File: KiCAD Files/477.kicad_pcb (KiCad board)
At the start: 2 copper layers, 53 parts, among them IC1 W25N01GVSFIG, IC2 W25N01GVSFIG, IC3 W25N01GVSFIG, IC4 W25N01GVSFIG, IC5 AZ1117IH-3.3TRG1, J1 BM06B-SRSS-TBT_LF__SN_, J2 6364372-2, J3 TSW-103-14-S-D, J4 TSW-103-14-S-D, U1 STM32H7A3RGTx, Y1 ABM8G-48.000MHZ-18-D2Y-T

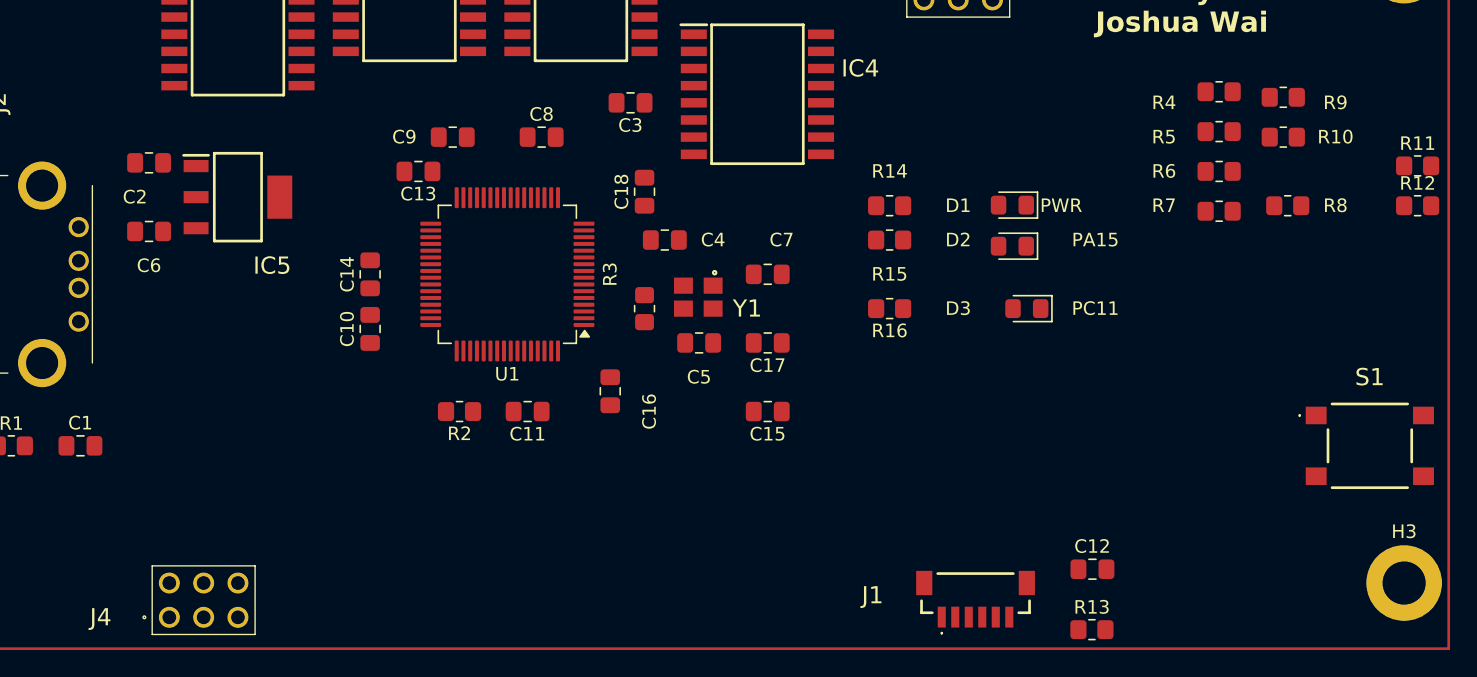
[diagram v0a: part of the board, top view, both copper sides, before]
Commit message: added additional connector
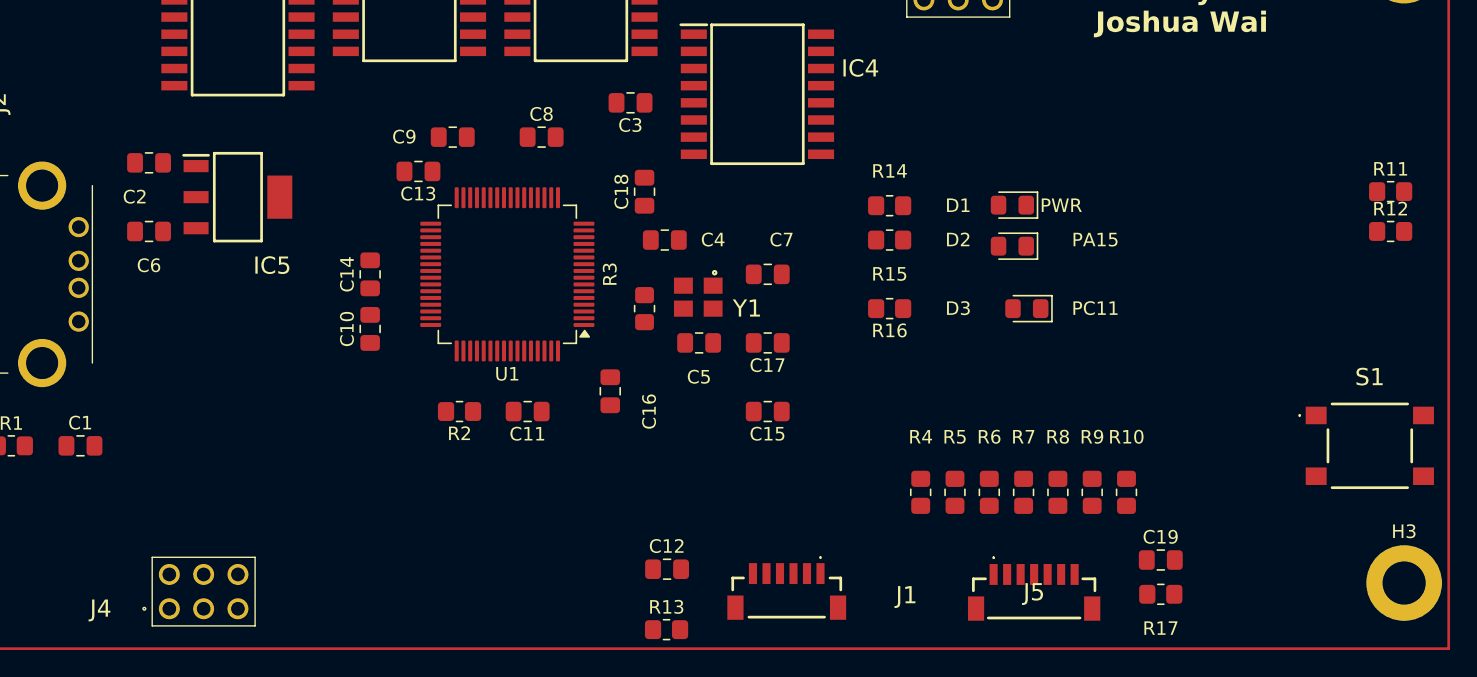
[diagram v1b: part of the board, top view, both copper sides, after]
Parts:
- added C19: 2.2n, Capacitor_SMD:C_0805_2012Metric_Pad1.18x1.45mm_HandSolder, F.Cu at (144.5, 110.7)
- added J5: BM07B-SRSS-TB_LF__SN_, CustomFootprints:BM07BSRSSTBLFSN, F.Cu at (135.2, 113.5)
- added R17: 1M, Resistor_SMD:R_0805_2012Metric_Pad1.20x1.40mm_HandSolder, F.Cu at (144.5, 113.2)
- C3: value C -> 0.1u
- moved R4 37.0 mm to (126.8, 105.7), turned to 90 degrees
- moved R5 33.1 mm to (129.3, 105.7), turned to 90 degrees
- moved R9 32.5 mm to (139.5, 105.7), turned to 90 degrees
- moved R13 31.5 mm to (107.9, 115.8)
- moved C12 31.5 mm to (108.0, 111.4)
- moved R6 29.2 mm to (131.8, 105.7), turned to 90 degrees
- moved R10 28.8 mm to (142.0, 105.7), turned to -90 degrees
- moved R8 27.2 mm to (136.9, 105.7), turned to -90 degrees
- moved R7 25.4 mm to (134.4, 105.7), turned to -90 degrees
- moved J1 14.0 mm to (116.8, 113.3), turned to 180 degrees
- moved R11 2.76 mm to (161.6, 83.4)
- moved R12 2.76 mm to (161.6, 86.4)
- moved J4 0.64 mm to (71.1, 114.3)
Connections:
- J1 pad 2: GND -> PC0/Touch Out
- J1 pad 3: PD2/FP RX -> VBAT
- J1 pad 5: VBAT -> PD2/FP RX
- J4 pad 1: unconnected-(J4-Pad1) -> PC0/Touch Out
- R10 pad 1: Net-(U7-Col3) -> PB6/KeyC3
- R10 pad 2: PB6/KeyC3 -> Net-(J5-Pad7)
- R7 pad 1: Net-(U7-Row4) -> PB3/KeyR4
- R7 pad 2: PB3/KeyR4 -> Net-(J5-Pad4)
- R8 pad 1: Net-(U7-Col1) -> PB4/KeyC1
- R8 pad 2: PB4/KeyC1 -> Net-(J5-Pad5)
- U1 pad 8: unconnected-(U1-PC0-Pad8) -> PC0/Touch Out

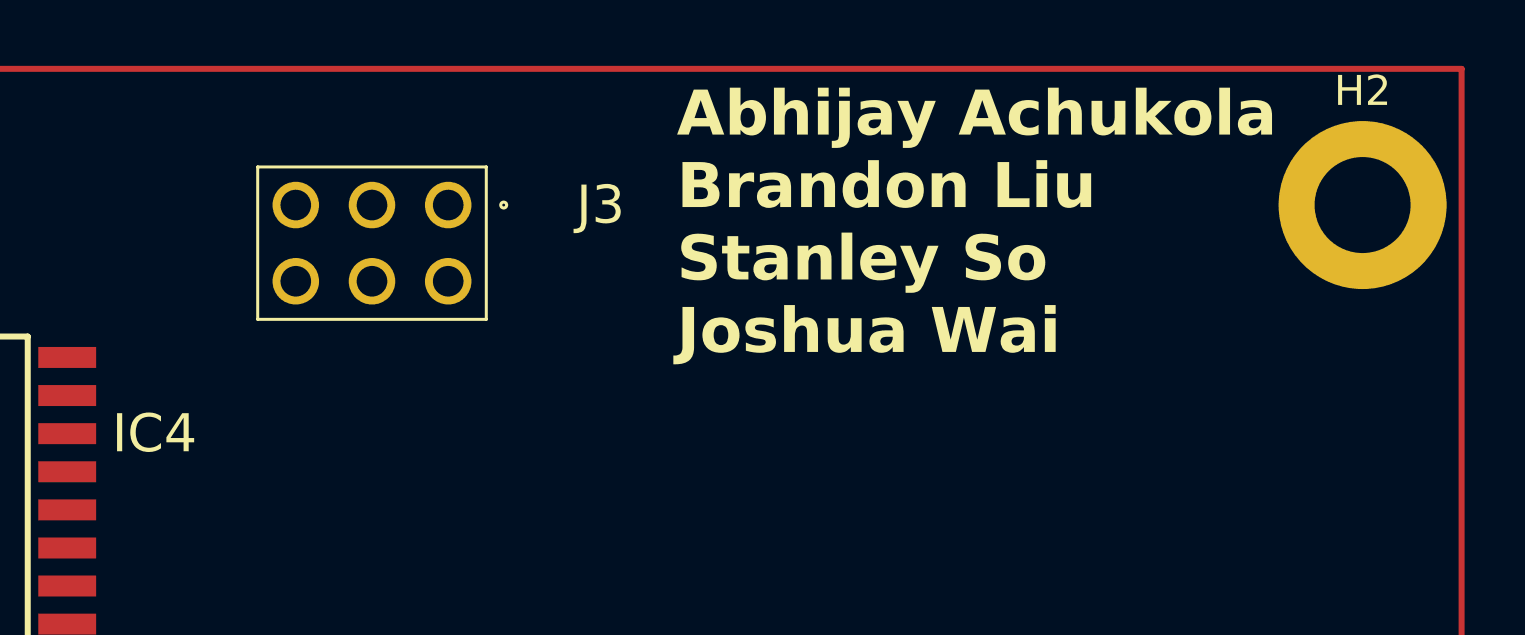
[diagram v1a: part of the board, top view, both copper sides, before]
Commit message: modified silkscreen
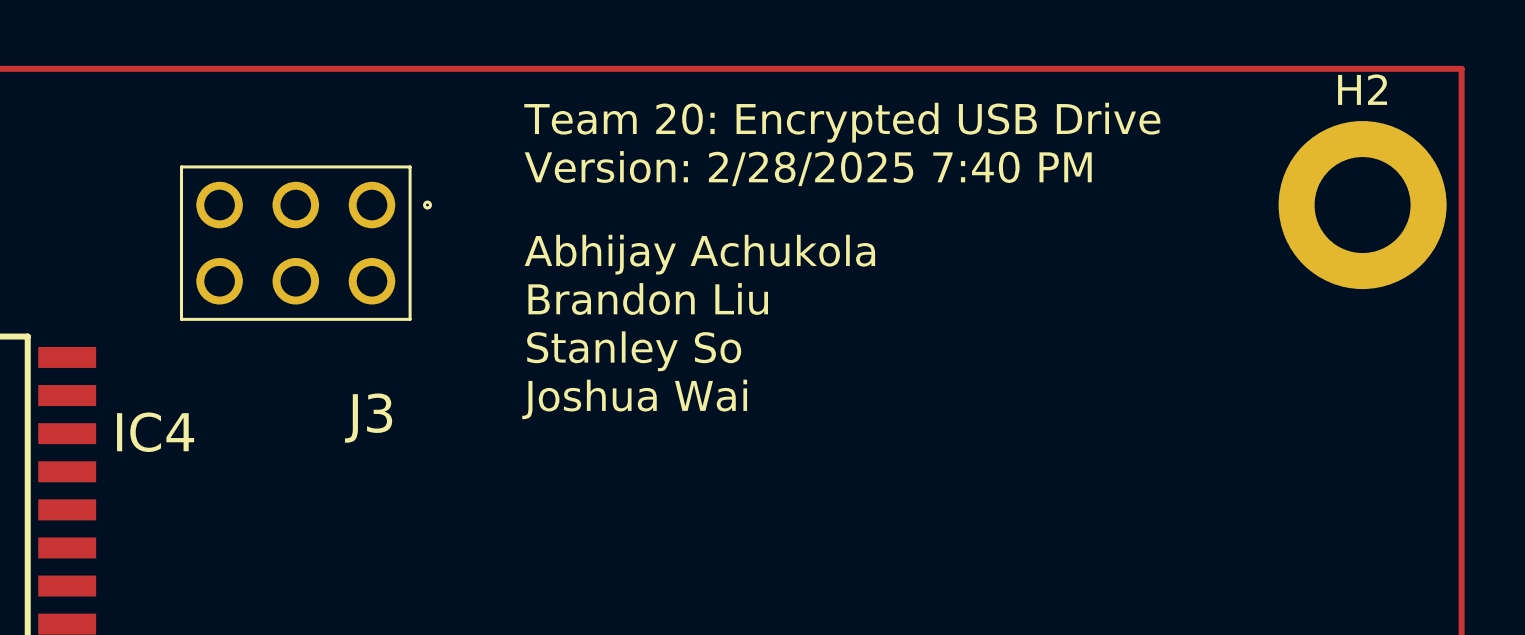
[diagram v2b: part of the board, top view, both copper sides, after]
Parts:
- moved J3 2.54 mm to (129.5, 66.7)
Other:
- board text added: "Team 20: Encrypted USB Drive Version: 2/28/2025 7:40 PM"
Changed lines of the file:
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@@
 	(footprint "CustomFootprints:custom1"
 		(layer "F.Cu")
-		(at 132.08 66.675 180)
+		(at 129.54 66.675 180)
 		(descr "TSW-103-XX-YY-D")
 		(tags "Connector")
 		(property "Reference" "J3"
-			(at -5.08 0 360)
+			(at 0 -6.985 360)
 			(layer "F.SilkS")
 			(effects
@@
 		)
 	)
-	(gr_text "Abhijay Achukola\nBrandon Liu\nStanley So \nJoshua Wai"
-		(at 139.7 71.755 0)
+	(gr_text "Team 20: Encrypted USB Drive\nVersion: 2/28/2025 7:40 PM\n"
+		(at 134.62 66.04 0)
 		(layer "F.SilkS")
 		(effects
 			(font
-				(size 1.5 1.5)
-				(thickness 0.3)
-				(bold yes)
+				(size 1 1)
+				(thickness 0.1875)
 			)
 			(justify left bottom)
@@
 		)
 	)
+	(gr_text "\nAbhijay Achukola\nBrandon Liu\nStanley So \nJoshua Wai"
+		(at 134.62 73.66 0)
+		(layer "F.SilkS")
+		(effects
+			(font
+				(size 1 1)
+				(thickness 0.125)
+			)
+			(justify left bottom)
+		)
+	)

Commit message: found final connector
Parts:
- removed R12: R_US, Resistor_SMD:R_0805_2012Metric_Pad1.20x1.40mm_HandSolder
- added C20: 2.2n, Capacitor_SMD:C_0805_2012Metric_Pad1.18x1.45mm_HandSolder, F.Cu at (138.9, 89.0)
- added J6: BM09B-SRSS-TB_LF__SN_, CustomFootprints:BM09BSRSSTBLFSN, F.Cu at (142.2, 78.7)
- R11: value R_US -> 1M
- moved S1 83.9 mm to (76.2, 99.1)
- moved H2 20.3 mm to (142.2, 66.0)
- moved H3 20.3 mm to (142.2, 111.8)
- moved R11 19.4 mm to (143.0, 89.0)
- moved C12 19.1 mm to (88.9, 109.8)
- moved J1 19.1 mm to (97.8, 111.8)
- moved R13 19.1 mm to (88.9, 114.3)
- moved J5 13.4 mm to (121.9, 111.8)
- moved C19 13.4 mm to (131.3, 108.9)
- moved R17 13.4 mm to (131.3, 111.5)
- moved R14 12.2 mm to (132.1, 94.0), turned to 90 degrees
- moved R5 10.1 mm to (119.4, 103.9)
- moved R9 10.1 mm to (129.5, 103.9)
- moved R4 10.1 mm to (116.8, 103.9)
- moved R6 10.1 mm to (121.9, 103.9)
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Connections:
- R11 pad 1: VBAT -> Net-(C20-Pad1)
- R11 pad 2: Net-(DS1-VO) -> GND
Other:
- board text added: "Team 20: Encrypted USB Drive Version: 2/28/2025 9:35 PM"
- board text removed: "Team 20: Encrypted USB Drive Version: 2/28/2025 7:40 PM"

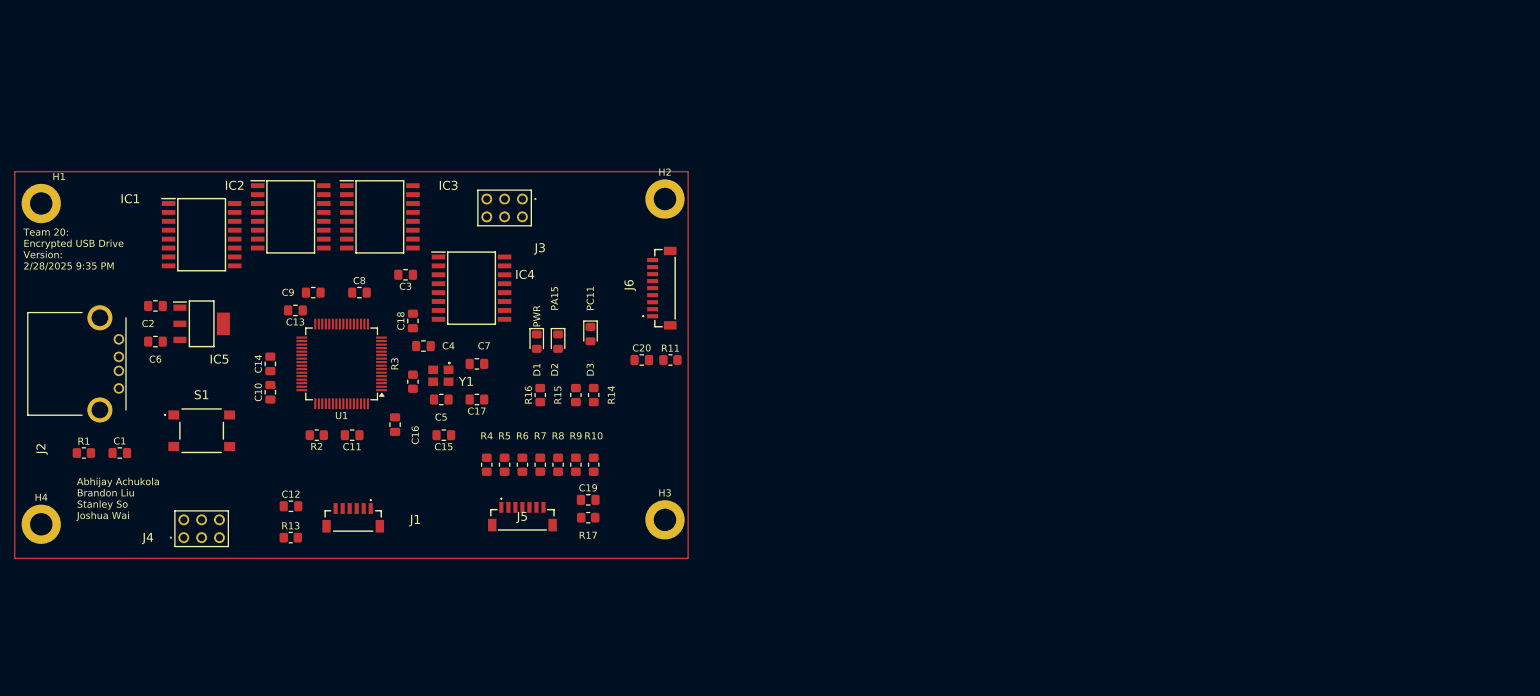
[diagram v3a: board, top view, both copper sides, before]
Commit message: finalized schematic
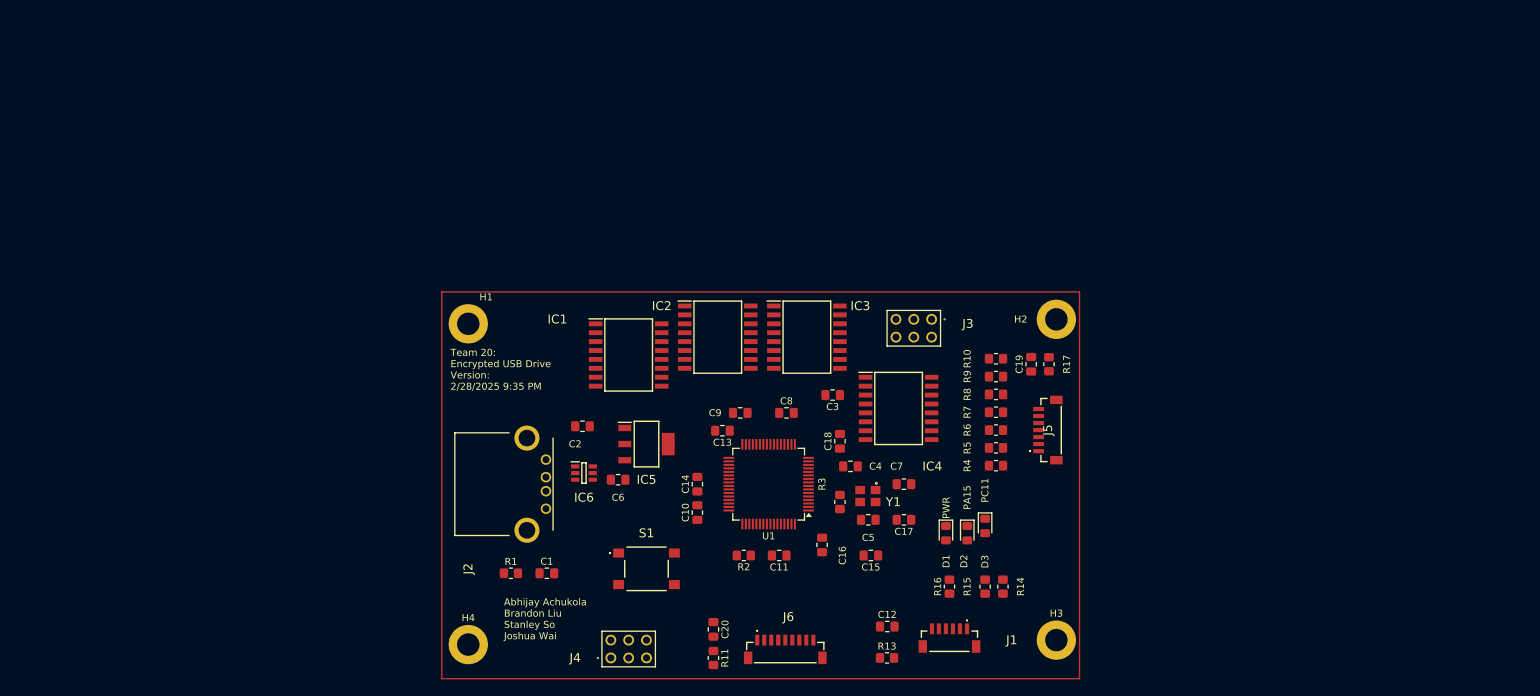
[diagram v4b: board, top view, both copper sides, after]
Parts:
- added IC6: USBLC6-2SC6, CustomFootprints:SOT95P280X145-6N, F.Cu at (130.7, 105.1)
- R14, R15, R16: value R_US -> 220
- R2: value R_US -> 10k
- moved C12 86.7 mm to (173.9, 127.0)
- moved J1 86.7 mm to (182.8, 128.9)
- moved R13 86.7 mm to (173.9, 131.4)
- moved J5 76.4 mm to (197.3, 99.0), turned to 90 degrees
- moved R4 72.6 mm to (189.4, 104.0), turned to 180 degrees
- moved R5 70.1 mm to (189.4, 101.5), turned to 180 degrees
- moved R17 69.2 mm to (197.0, 89.6), turned to 90 degrees
- moved C6 68.8 mm to (135.6, 106.0)
- moved R6 67.7 mm to (189.4, 99.0), turned to 180 degrees
- moved S1 66.4 mm to (139.6, 118.7)
- moved C19 66.0 mm to (194.4, 89.6), turned to 90 degrees
- moved IC5 65.7 mm to (139.6, 101.0)
- moved R7 65.4 mm to (189.4, 96.4), turned to 0 degrees
- moved D1 64.4 mm to (182.3, 113.7)
- moved R15 64.4 mm to (187.9, 121.3)
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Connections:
- J2 pad 2: PA11/USB- -> Net-(IC6-I/O1_1)
- J2 pad 3: PA12/USB+ -> Net-(IC6-I/O2_1)

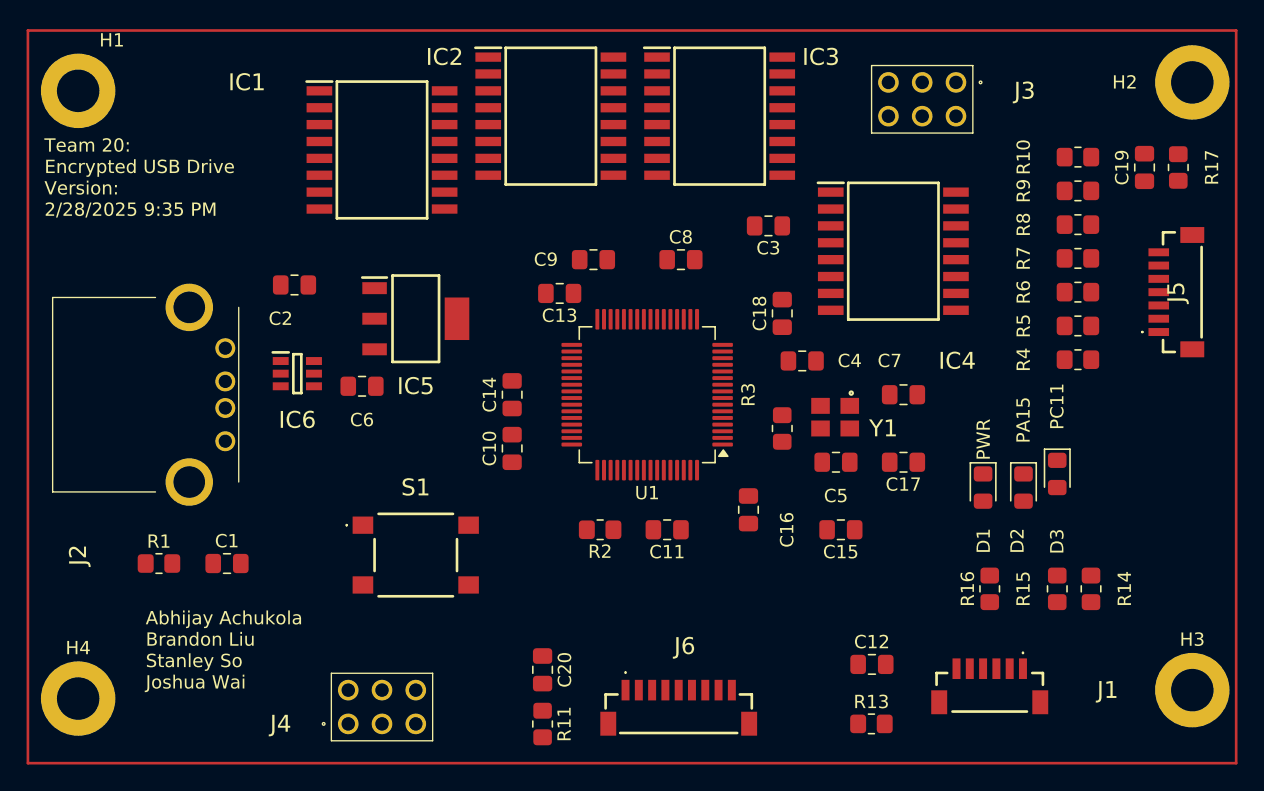
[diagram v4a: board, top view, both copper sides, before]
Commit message: modified mounting holes
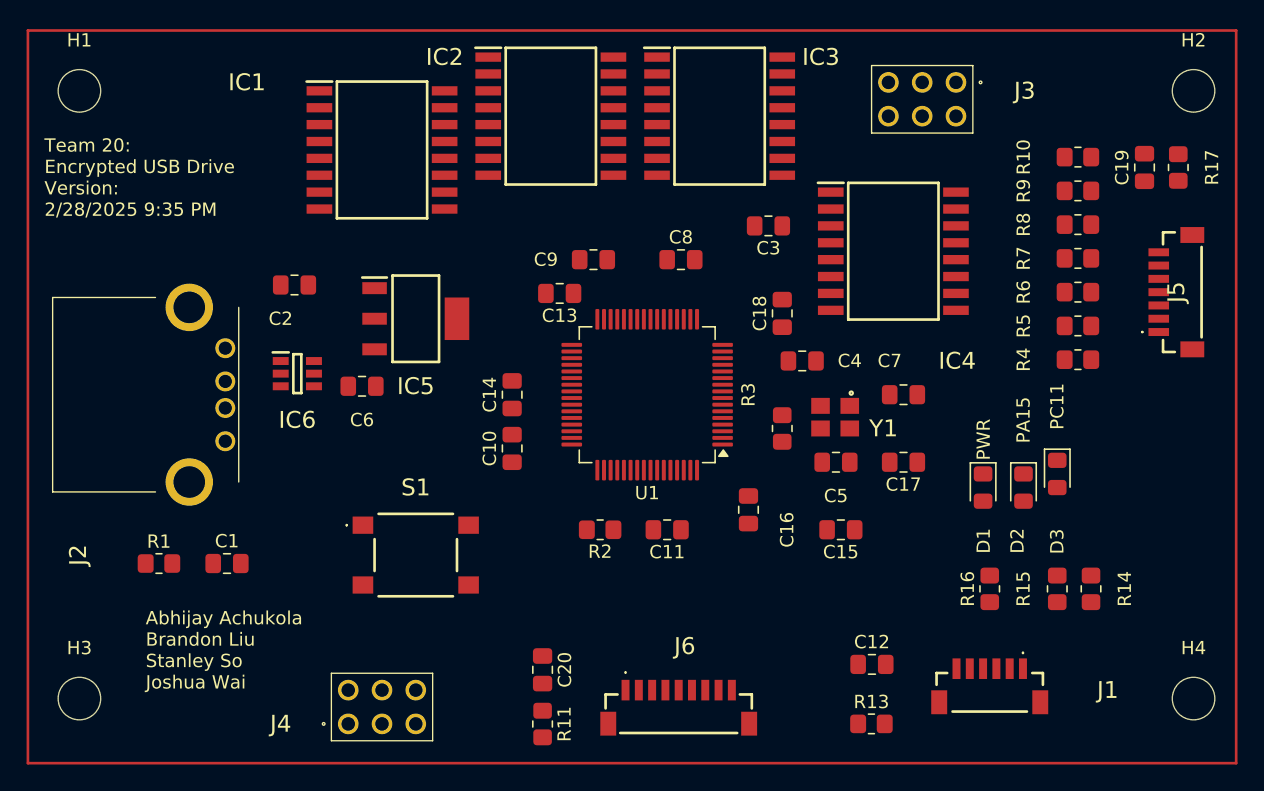
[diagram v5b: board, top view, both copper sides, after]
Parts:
- H1, H2, H3, H4: value MountingHole_Pad -> MountingHole; footprint MountingHole:MountingHole_3.2mm_M3_DIN965_Pad -> MountingHole:MountingHole_3.2mm_M3_DIN965
- moved H4 83.9 mm to (198.1, 129.5)
- moved H3 83.7 mm to (114.3, 129.5)
- moved H2 0.64 mm to (198.1, 83.8)
- moved H1 0.09 mm to (114.3, 83.8)
